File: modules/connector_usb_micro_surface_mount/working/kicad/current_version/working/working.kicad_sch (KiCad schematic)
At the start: 1 part, among them J1 scumcsm

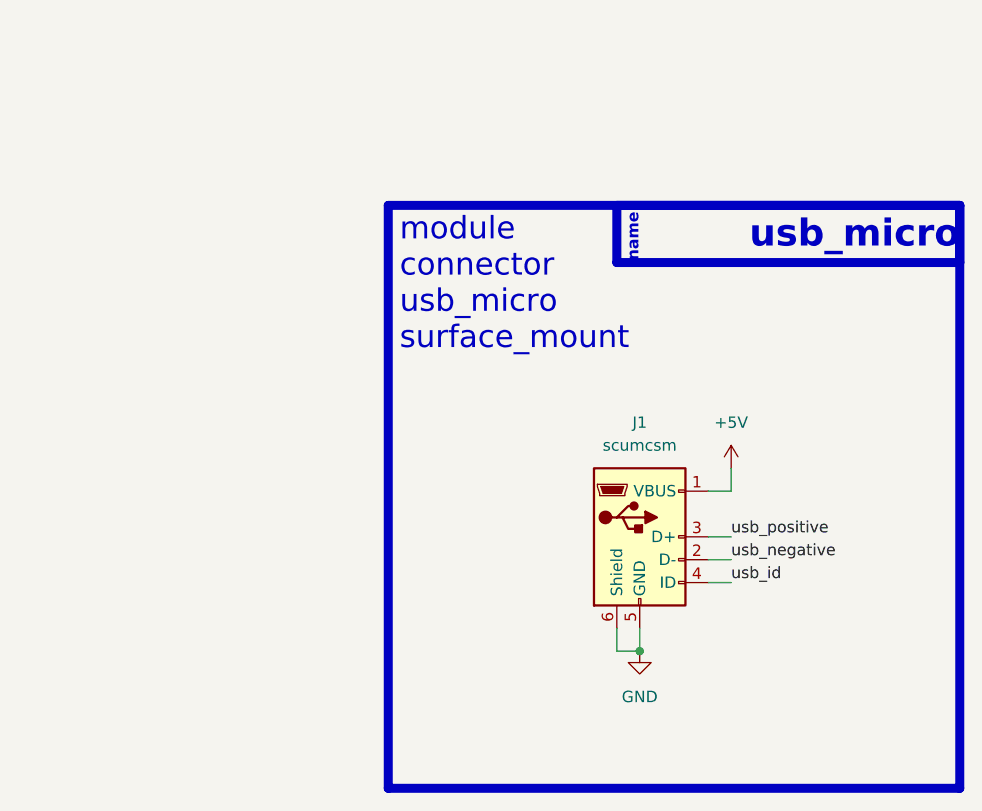
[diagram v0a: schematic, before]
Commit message: fixed formatting to be more consistent
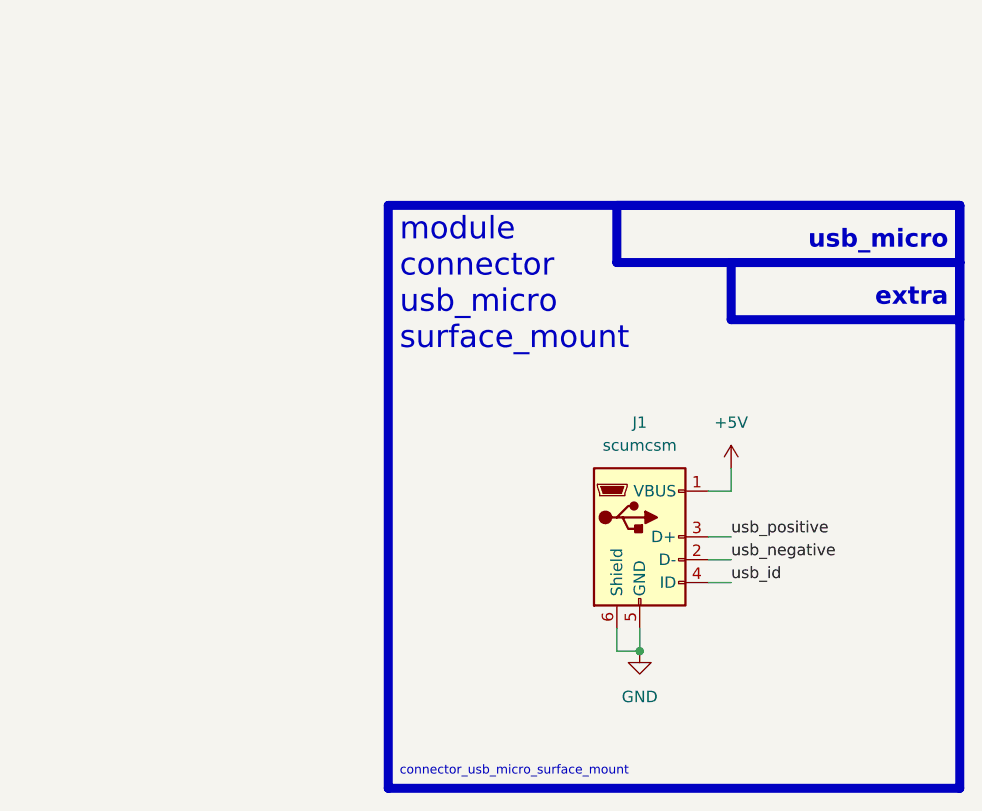
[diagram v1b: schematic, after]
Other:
- note added: "connector_usb_micro_surface_mount"
- note added: "extra"
- note removed: "name"
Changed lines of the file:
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@@
   (rectangle (start 139.7 54.61) (end 177.8 60.96)
     (stroke (width 1) (type default))
-    (fill (type color) (color 0 0 0 0))
+    (fill (type none))
   )
-  (text "usb_micro" (at 177.8 59.69 0)
-    (effects (font (size 3 3) (thickness 0.8) bold (color 255 255 255 1)) (justify right bottom))
+  (rectangle (start 152.4 60.96) (end 177.8 67.31)
+    (stroke (width 1) (type default))
+    (fill (type none))
   )
-  (text "name" (at 142.24 60.96 90)
-    (effects (font (size 1.27 1.27) (thickness 0.254) bold (color 255 255 255 1)) (justify left bottom))
+  (text "usb_micro" (at 176.53 59.69 0)
+    (effects (font (size 2 2) (thickness 0.8) bold) (justify right bottom))
+  )
+  (text "extra" (at 176.53 66.04 0)
+    (effects (font (size 2 2) (thickness 0.8) bold) (justify right bottom))
+  )
+  (text "connector_usb_micro_surface_mount" (at 115.57 118.11 0)
+    (effects (font (size 1 1)) (justify left bottom))
   )
   (text "module\nconnector\nusb_micro\nsurface_mount\n\n" (at 115.57 74.93 0)

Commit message: a few fix ups
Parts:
- renumbered J1 to CON1
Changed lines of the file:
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@@
   (symbol (lib_id "oomlout_oomp_part_symbols:scumcsm_electronic_socket_usb_micro_surface_mount") (at 142.24 91.44 0) (unit 1)
     (in_bom yes) (on_board yes) (dnp no) (fields_autoplaced)
-    (property "Reference" "J1" (at 142.24 78.74 0)
+    (property "Reference" "CON1" (at 142.24 78.74 0)
       (effects (font (size 1.27 1.27)))
     )
@@
       (project "working"
         (path "/c9993764-076f-44f6-bf4c-6b69ce17c9e4"
-          (reference "J1") (unit 1)
+          (reference "CON1") (unit 1)
         )
       )

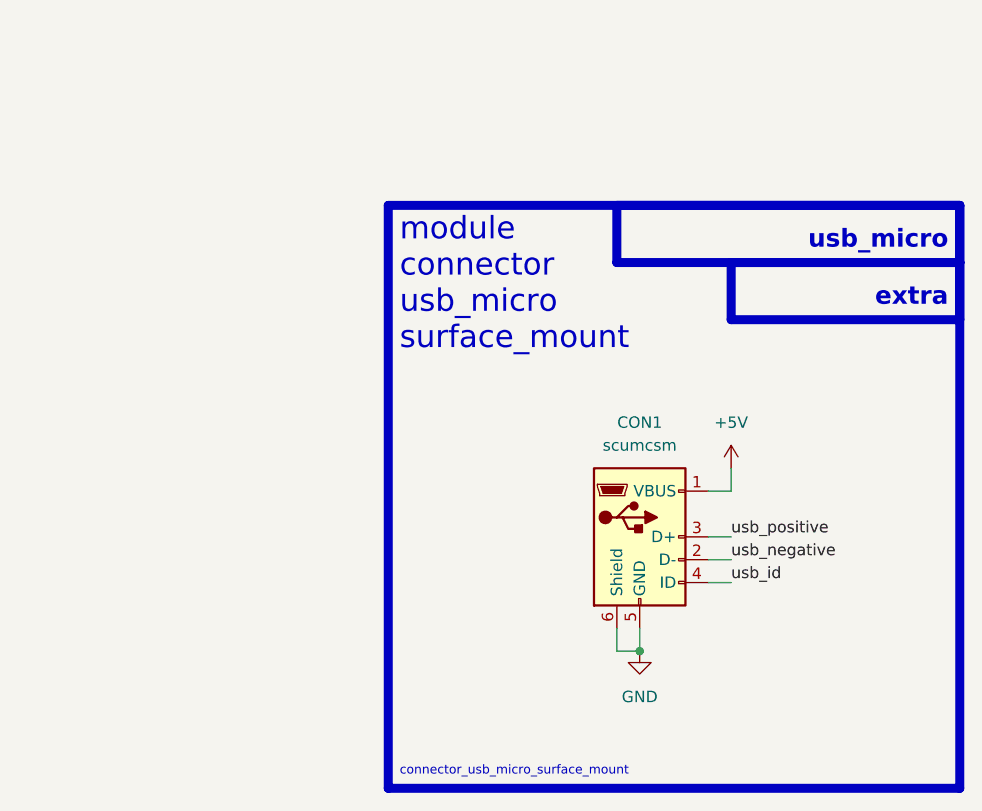
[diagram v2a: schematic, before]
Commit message: schematic formatting
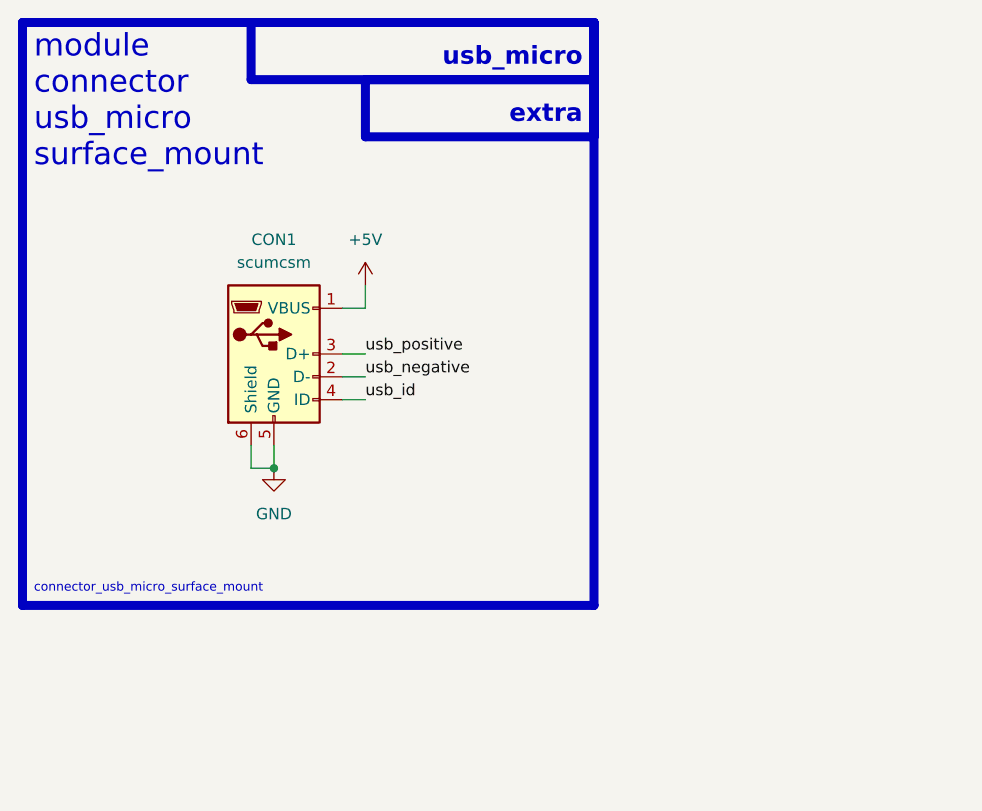
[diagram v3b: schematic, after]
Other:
- moved on the sheet: CON1
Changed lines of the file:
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@@
 (kicad_sch (version 20230121) (generator eeschema)
-  (paper "A4")
-  (junction (at 142.24 104.14) (diameter 0) (color 0 0 0 0)
+  (paper "A5")
+  (junction (at 101.6 83.82) (diameter 0) (color 0 0 0 0)
   )
-  (wire (pts (xy 152.4 83.82) (xy 152.4 86.36))
+  (wire (pts (xy 111.76 63.5) (xy 111.76 66.04))
     (stroke (width 0) (type default))
   )
-  (wire (pts (xy 139.7 104.14) (xy 142.24 104.14))
+  (wire (pts (xy 99.06 83.82) (xy 101.6 83.82))
     (stroke (width 0) (type default))
   )
-  (wire (pts (xy 142.24 101.6) (xy 142.24 104.14))
+  (wire (pts (xy 101.6 81.28) (xy 101.6 83.82))
     (stroke (width 0) (type default))
   )
-  (wire (pts (xy 149.86 86.36) (xy 152.4 86.36))
+  (wire (pts (xy 109.22 66.04) (xy 111.76 66.04))
     (stroke (width 0) (type default))
   )
-  (wire (pts (xy 149.86 96.52) (xy 152.4 96.52))
+  (wire (pts (xy 109.22 76.2) (xy 111.76 76.2))
     (stroke (width 0) (type default))
   )
-  (wire (pts (xy 149.86 91.44) (xy 152.4 91.44))
+  (wire (pts (xy 109.22 71.12) (xy 111.76 71.12))
     (stroke (width 0) (type default))
   )
-  (wire (pts (xy 149.86 93.98) (xy 152.4 93.98))
+  (wire (pts (xy 109.22 73.66) (xy 111.76 73.66))
     (stroke (width 0) (type default))
   )
-  (wire (pts (xy 139.7 101.6) (xy 139.7 104.14))
+  (wire (pts (xy 99.06 81.28) (xy 99.06 83.82))
     (stroke (width 0) (type default))
   )
-  (rectangle (start 114.3 54.61) (end 177.8 119.38)
+  (rectangle (start 73.66 34.29) (end 137.16 99.06)
     (stroke (width 1) (type default))
     (fill (type none))
   )
-  (rectangle (start 139.7 54.61) (end 177.8 60.96)
+  (rectangle (start 99.06 34.29) (end 137.16 40.64)
     (stroke (width 1) (type default))
     (fill (type none))
   )
-  (rectangle (start 152.4 60.96) (end 177.8 67.31)
+  (rectangle (start 111.76 40.64) (end 137.16 46.99)
     (stroke (width 1) (type default))
     (fill (type none))
   )
-  (text "usb_micro" (at 176.53 59.69 0)
+  (text "usb_micro" (at 135.89 39.37 0)
     (effects (font (size 2 2) (thickness 0.8) bold) (justify right bottom))
   )
-  (text "extra" (at 176.53 66.04 0)
+  (text "extra" (at 135.89 45.72 0)
     (effects (font (size 2 2) (thickness 0.8) bold) (justify right bottom))
   )
-  (text "connector_usb_micro_surface_mount" (at 115.57 118.11 0)
+  (text "connector_usb_micro_surface_mount" (at 74.93 97.79 0)
     (effects (font (size 1 1)) (justify left bottom))
   )
-  (text "module\nconnector\nusb_micro\nsurface_mount\n\n" (at 115.57 74.93 0)
+  (text "module\nconnector\nusb_micro\nsurface_mount\n\n" (at 74.93 54.61 0)
     (effects (font (size 2.5 2.5)) (justify left bottom))
   )
-  (label "usb_id" (at 152.4 96.52 0) (fields_autoplaced)
+  (label "usb_id" (at 111.76 76.2 0) (fields_autoplaced)
     (effects (font (size 1.27 1.27)) (justify left bottom))
   )
-  (label "usb_positive" (at 152.4 91.44 0) (fields_autoplaced)
+  (label "usb_positive" (at 111.76 71.12 0) (fields_autoplaced)
     (effects (font (size 1.27 1.27)) (justify left bottom))
   )
-  (label "usb_negative" (at 152.4 93.98 0) (fields_autoplaced)
+  (label "usb_negative" (at 111.76 73.66 0) (fields_autoplaced)
     (effects (font (size 1.27 1.27)) (justify left bottom))
   )
-  (symbol (lib_id "power:GND") (at 142.24 104.14 0) (unit 1)
+  (symbol (lib_id "power:GND") (at 101.6 83.82 0) (unit 1)
     (in_bom yes) (on_board yes) (dnp no) (fields_autoplaced)
-    (property "Reference" "#PWR012" (at 142.24 110.49 0)
+    (property "Reference" "#PWR012" (at 101.6 90.17 0)
       (effects (font (size 1.27 1.27)) hide)
     )
-    (property "Value" "GND" (at 142.24 109.22 0)
+    (property "Value" "GND" (at 101.6 88.9 0)
       (effects (font (size 1.27 1.27)))
     )
-    (property "Footprint" "" (at 142.24 104.14 0)
+    (property "Footprint" "" (at 101.6 83.82 0)
       (effects (font (size 1.27 1.27)) hide)
     )
-    (property "Datasheet" "" (at 142.24 104.14 0)
+    (property "Datasheet" "" (at 101.6 83.82 0)
       (effects (font (size 1.27 1.27)) hide)
     )
@@
     )
   )
-  (symbol (lib_id "oomlout_oomp_part_symbols:scumcsm_electronic_socket_usb_micro_surface_mount") (at 142.24 91.44 0) (unit 1)
+  (symbol (lib_id "oomlout_oomp_part_symbols:scumcsm_electronic_socket_usb_micro_surface_mount") (at 101.6 71.12 0) (unit 1)
     (in_bom yes) (on_board yes) (dnp no) (fields_autoplaced)
-    (property "Reference" "CON1" (at 142.24 78.74 0)
+    (property "Reference" "CON1" (at 101.6 58.42 0)
       (effects (font (size 1.27 1.27)))
     )
-    (property "Value" "scumcsm" (at 142.24 81.28 0)
+    (property "Value" "scumcsm" (at 101.6 60.96 0)
       (effects (font (size 1.27 1.27)))
     )
-    (property "Footprint" "oomlout_oomp_part_footprints:scumcsm_electronic_socket_usb_micro_surface_mount" (at 146.05 92.71 0)
+    (property "Footprint" "oomlout_oomp_part_footprints:scumcsm_electronic_socket_usb_micro_surface_mount" (at 105.41 72.39 0)
       (effects (font (size 1.27 1.27)) hide)
     )
-    (property "Datasheet" "https://github.com/oomlout/oomlout_oomp_v3/parts/electronic_socket_usb_micro_surface_mount/datasheet.pdf" (at 146.05 92.71 0)
+    (property "Datasheet" "https://github.com/oomlout/oomlout_oomp_v3/parts/electronic_socket_usb_micro_surface_mount/datasheet.pdf" (at 105.41 72.39 0)
       (effects (font (size 1.27 1.27)) hide)
     )
@@
     )
   )
-  (symbol (lib_id "power:+5V") (at 152.4 83.82 0) (unit 1)
+  (symbol (lib_id "power:+5V") (at 111.76 63.5 0) (unit 1)
     (in_bom yes) (on_board yes) (dnp no) (fields_autoplaced)
-    (property "Reference" "#PWR013" (at 152.4 87.63 0)
+    (property "Reference" "#PWR013" (at 111.76 67.31 0)
       (effects (font (size 1.27 1.27)) hide)
     )
-    (property "Value" "+5V" (at 152.4 78.74 0)
+    (property "Value" "+5V" (at 111.76 58.42 0)
       (effects (font (size 1.27 1.27)))
     )
-    (property "Footprint" "" (at 152.4 83.82 0)
+    (property "Footprint" "" (at 111.76 63.5 0)
       (effects (font (size 1.27 1.27)) hide)
     )
-    (property "Datasheet" "" (at 152.4 83.82 0)
+    (property "Datasheet" "" (at 111.76 63.5 0)
       (effects (font (size 1.27 1.27)) hide)
     )
